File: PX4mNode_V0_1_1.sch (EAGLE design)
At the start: 133 parts, among them J201 DF13C-6P-1.25V, J202 DF13C-6P-1.25V, J203 DF13C-6P-1.25V, J301 DF13C-4P-1.25V, J401 DF13C-7P-1.25V, J402 DF13-4P-1.25V, J403 DF13C-4P-1.25V, J404 DF13C-4P-1.25V, J405 DF13C-4P-1.25V, J801 DF13C-3P-1.25V, M3_MOUNT1101 MOUNT-HOLE3.1MM, M3_MOUNT1102 MOUNT-HOLE3.1MM, M3_MOUNT1103 MOUNT-HOLE3.1MM, M3_MOUNT1104 MOUNT-HOLE3.1MM, U101 STM32F4X7VX, U401 MAX3051, U402 MAX3051, X101 3.2x2.5 mm / 24 MHz / 15 ppm

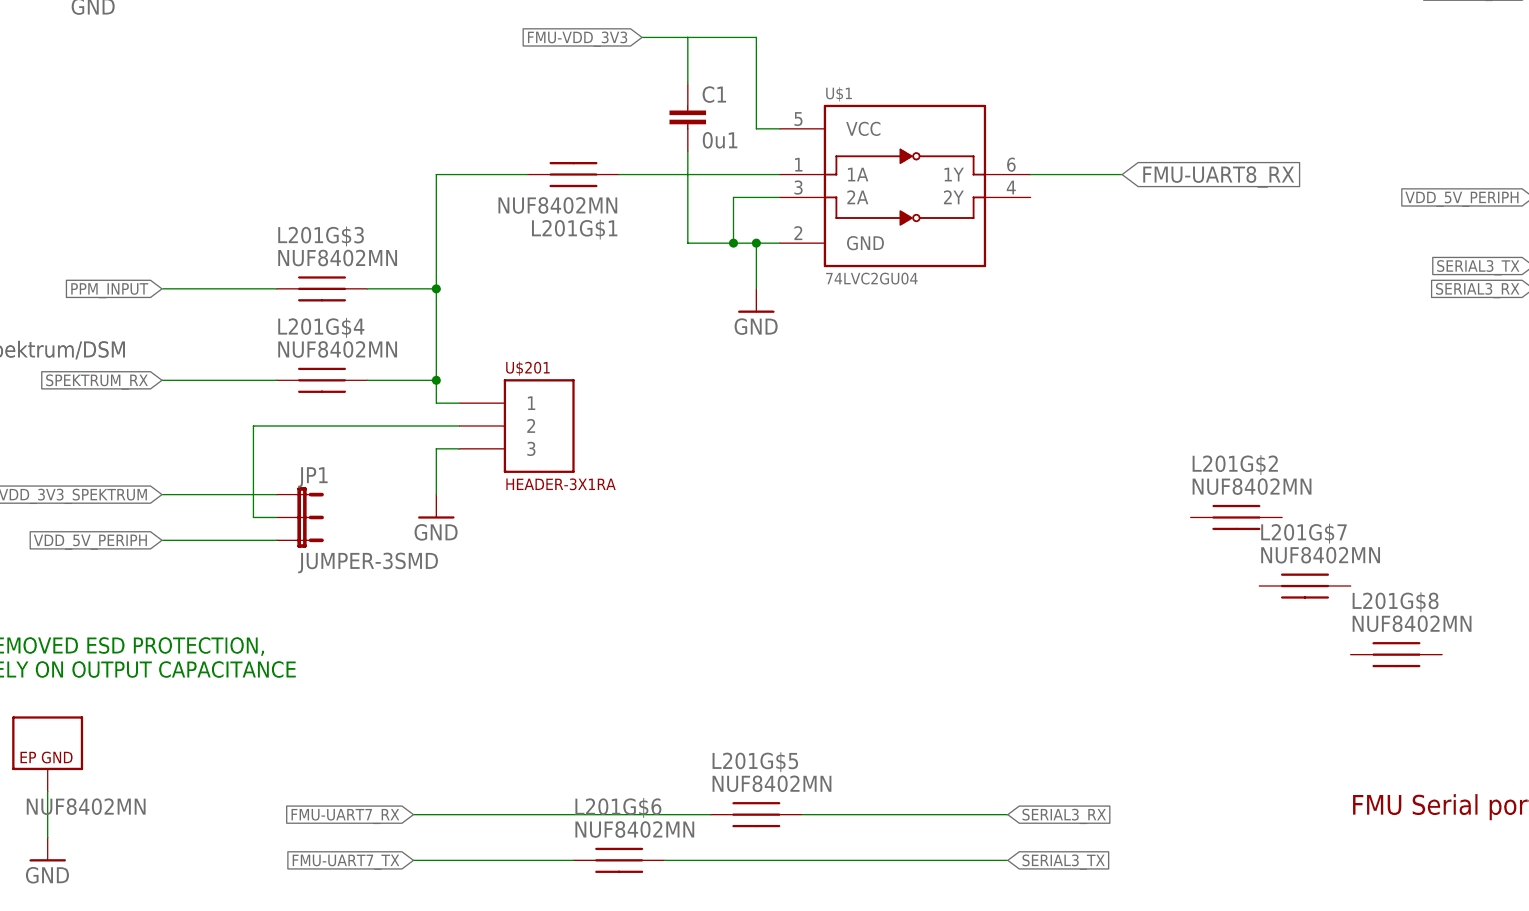
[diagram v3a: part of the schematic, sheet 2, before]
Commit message: Reworked sbus input to make space for sbus output
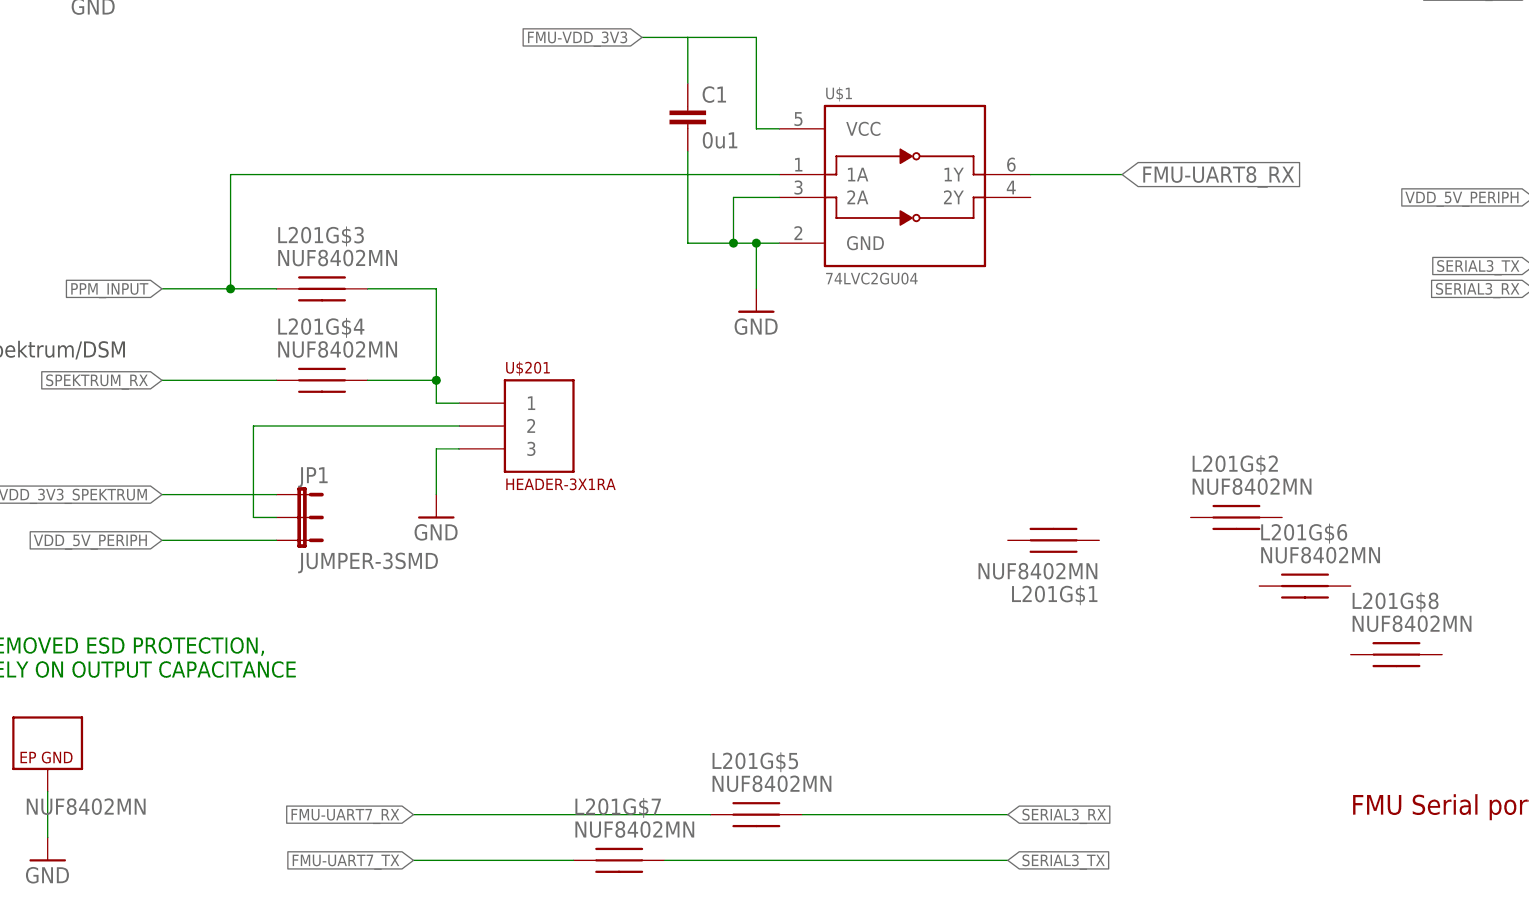
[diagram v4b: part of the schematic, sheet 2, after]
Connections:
- removed net N$5: L201G$1.P$1, U$1.1A
- net FMU-UART7_TX: now also L201G$7.P$1; no longer L201G$6.P$1
- net N$18: no longer L201G$1.P$2
- net PPM_INPUT: now also U$1.1A
- net SERIAL3_TX: now also L201G$7.P$2; no longer L201G$6.P$2
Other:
- moved on the sheet: L201G$1, L201G$6, L201G$7
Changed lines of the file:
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@@
 <instance part="L201" gate="G$9" x="20.32" y="20.32"/>
 <instance part="L201" gate="G$5" x="99.06" y="17.78"/>
-<instance part="L201" gate="G$6" x="83.82" y="12.7"/>
+<instance part="L201" gate="G$7" x="83.82" y="12.7"/>
 <instance part="L201" gate="G$3" x="50.8" y="76.2"/>
 <instance part="L201" gate="G$4" x="50.8" y="66.04"/>
@@
 <instance part="GND46" gate="1" x="63.5" y="50.8"/>
 <instance part="U$201" gate="G$1" x="73.66" y="58.42"/>
-<instance part="L201" gate="G$1" x="78.74" y="88.9" rot="R180"/>
-<instance part="L201" gate="G$7" x="160.02" y="43.18"/>
+<instance part="L201" gate="G$1" x="132.08" y="48.26" rot="R180"/>
+<instance part="L201" gate="G$6" x="160.02" y="43.18"/>
 <instance part="L201" gate="G$2" x="152.4" y="50.8"/>
 <instance part="L201" gate="G$8" x="170.18" y="35.56"/>
@@
 <segment>
 <label x="127" y="12.7" size="1.27" layer="95" xref="yes"/>
-<pinref part="L201" gate="G$6" pin="P$2"/>
+<pinref part="L201" gate="G$7" pin="P$2"/>
 <wire x1="127" y1="12.7" x2="88.9" y2="12.7" width="0.1524" layer="91"/>
 </segment>
@@
 <wire x1="63.5" y1="63.5" x2="63.5" y2="66.04" width="0.1524" layer="91"/>
 <junction x="63.5" y="66.04"/>
-<pinref part="L201" gate="G$1" pin="P$2"/>
-<wire x1="73.66" y1="88.9" x2="63.5" y2="88.9" width="0.1524" layer="91"/>
-<wire x1="63.5" y1="88.9" x2="63.5" y2="76.2" width="0.1524" layer="91"/>
-<junction x="63.5" y="76.2"/>
 </segment>
 </net>
@@
 <segment>
 <label x="33.02" y="76.2" size="1.27" layer="95" rot="R180" xref="yes"/>
-<wire x1="33.02" y1="76.2" x2="45.72" y2="76.2" width="0.1524" layer="91"/>
+<wire x1="33.02" y1="76.2" x2="40.64" y2="76.2" width="0.1524" layer="91"/>
 <pinref part="L201" gate="G$3" pin="P$1"/>
+<pinref part="U$1" gate="G$1" pin="1A"/>
+<wire x1="40.64" y1="76.2" x2="45.72" y2="76.2" width="0.1524" layer="91"/>
+<wire x1="101.6" y1="88.9" x2="40.64" y2="88.9" width="0.1524" layer="91"/>
+<wire x1="40.64" y1="88.9" x2="40.64" y2="76.2" width="0.1524" layer="91"/>
+<junction x="40.64" y="76.2"/>
 </segment>
 </net>
@@
 <segment>
 <label x="60.96" y="12.7" size="1.27" layer="95" rot="R180" xref="yes"/>
-<pinref part="L201" gate="G$6" pin="P$1"/>
+<pinref part="L201" gate="G$7" pin="P$1"/>
 <wire x1="78.74" y1="12.7" x2="60.96" y2="12.7" width="0.1524" layer="91"/>
 </segment>
 </net>
-<net name="N$5" class="0">
-<segment>
-<pinref part="L201" gate="G$1" pin="P$1"/>
-<pinref part="U$1" gate="G$1" pin="1A"/>
-<wire x1="83.82" y1="88.9" x2="101.6" y2="88.9" width="0.1524" layer="91"/>
-</segment>
-</net>
